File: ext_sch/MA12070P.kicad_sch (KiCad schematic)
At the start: 45 parts, among them J7 Screw Term.

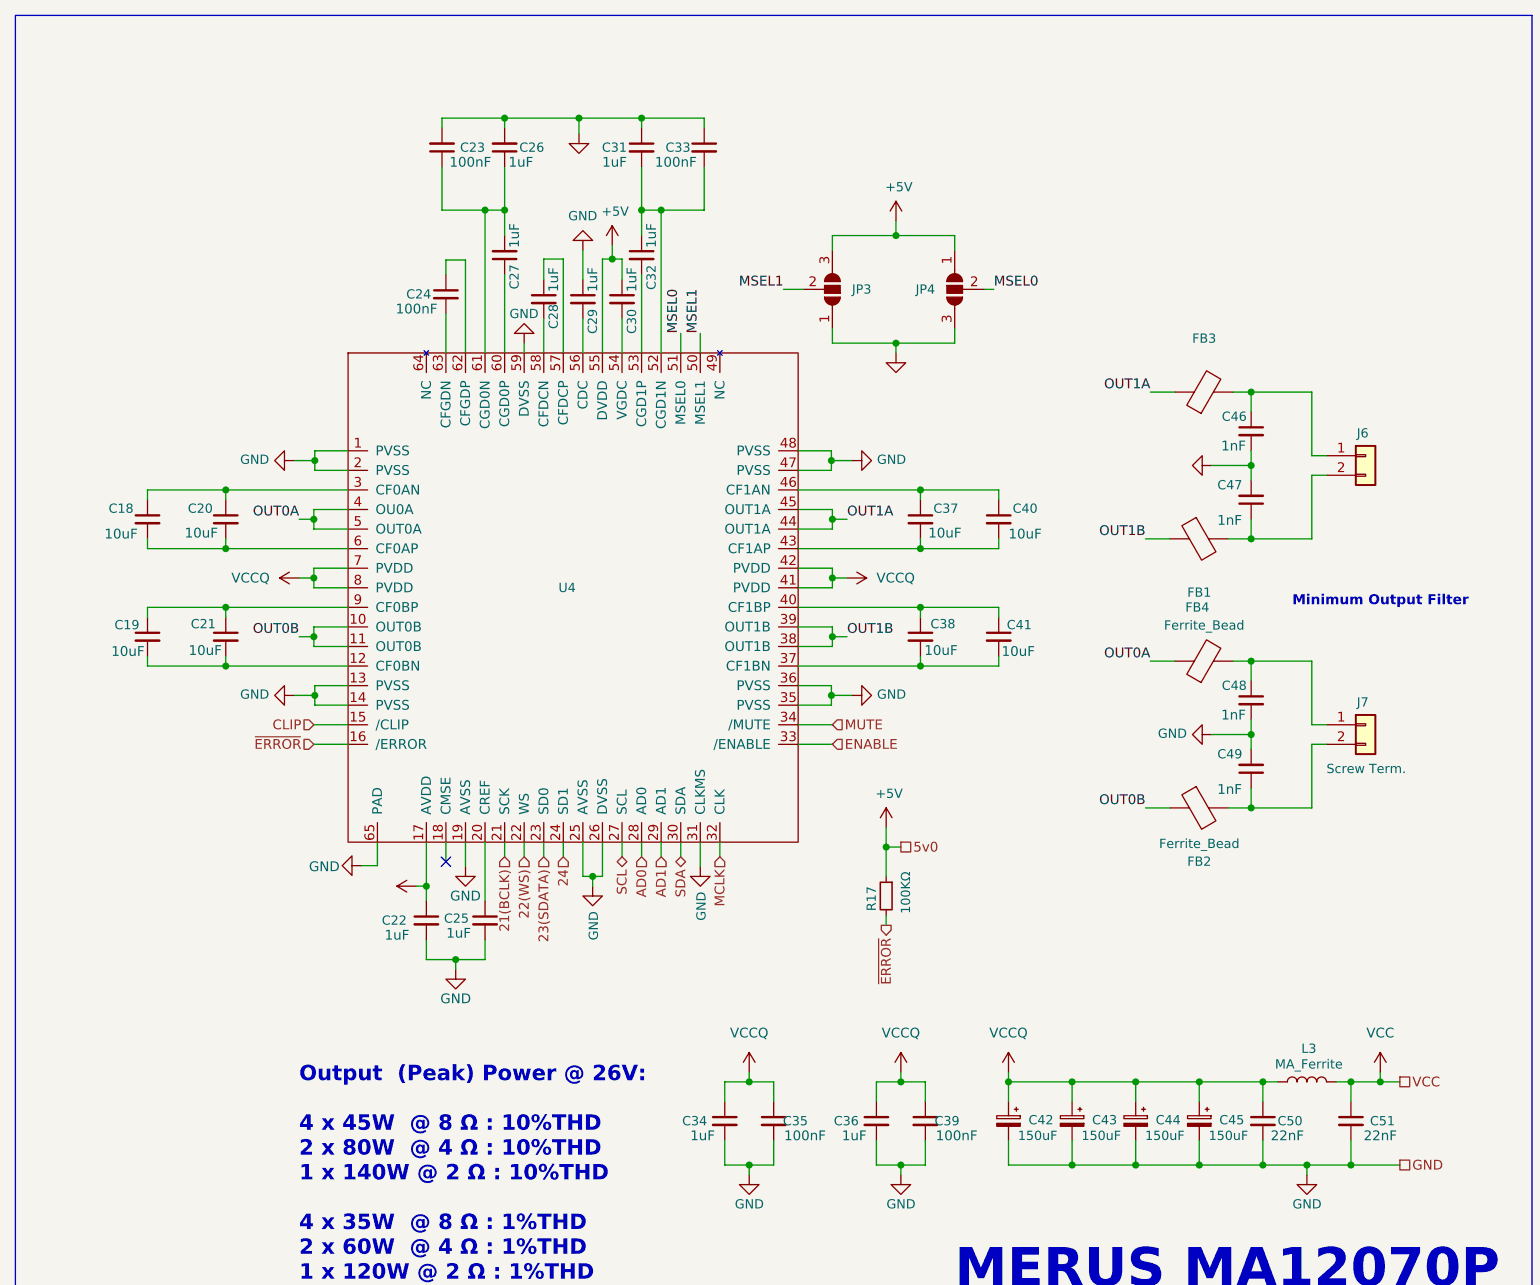
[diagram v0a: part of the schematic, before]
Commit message: Rev04 in the works. New changes include; New DCDC buck, two new connectors, replaced WS-diodes, removed err-diode
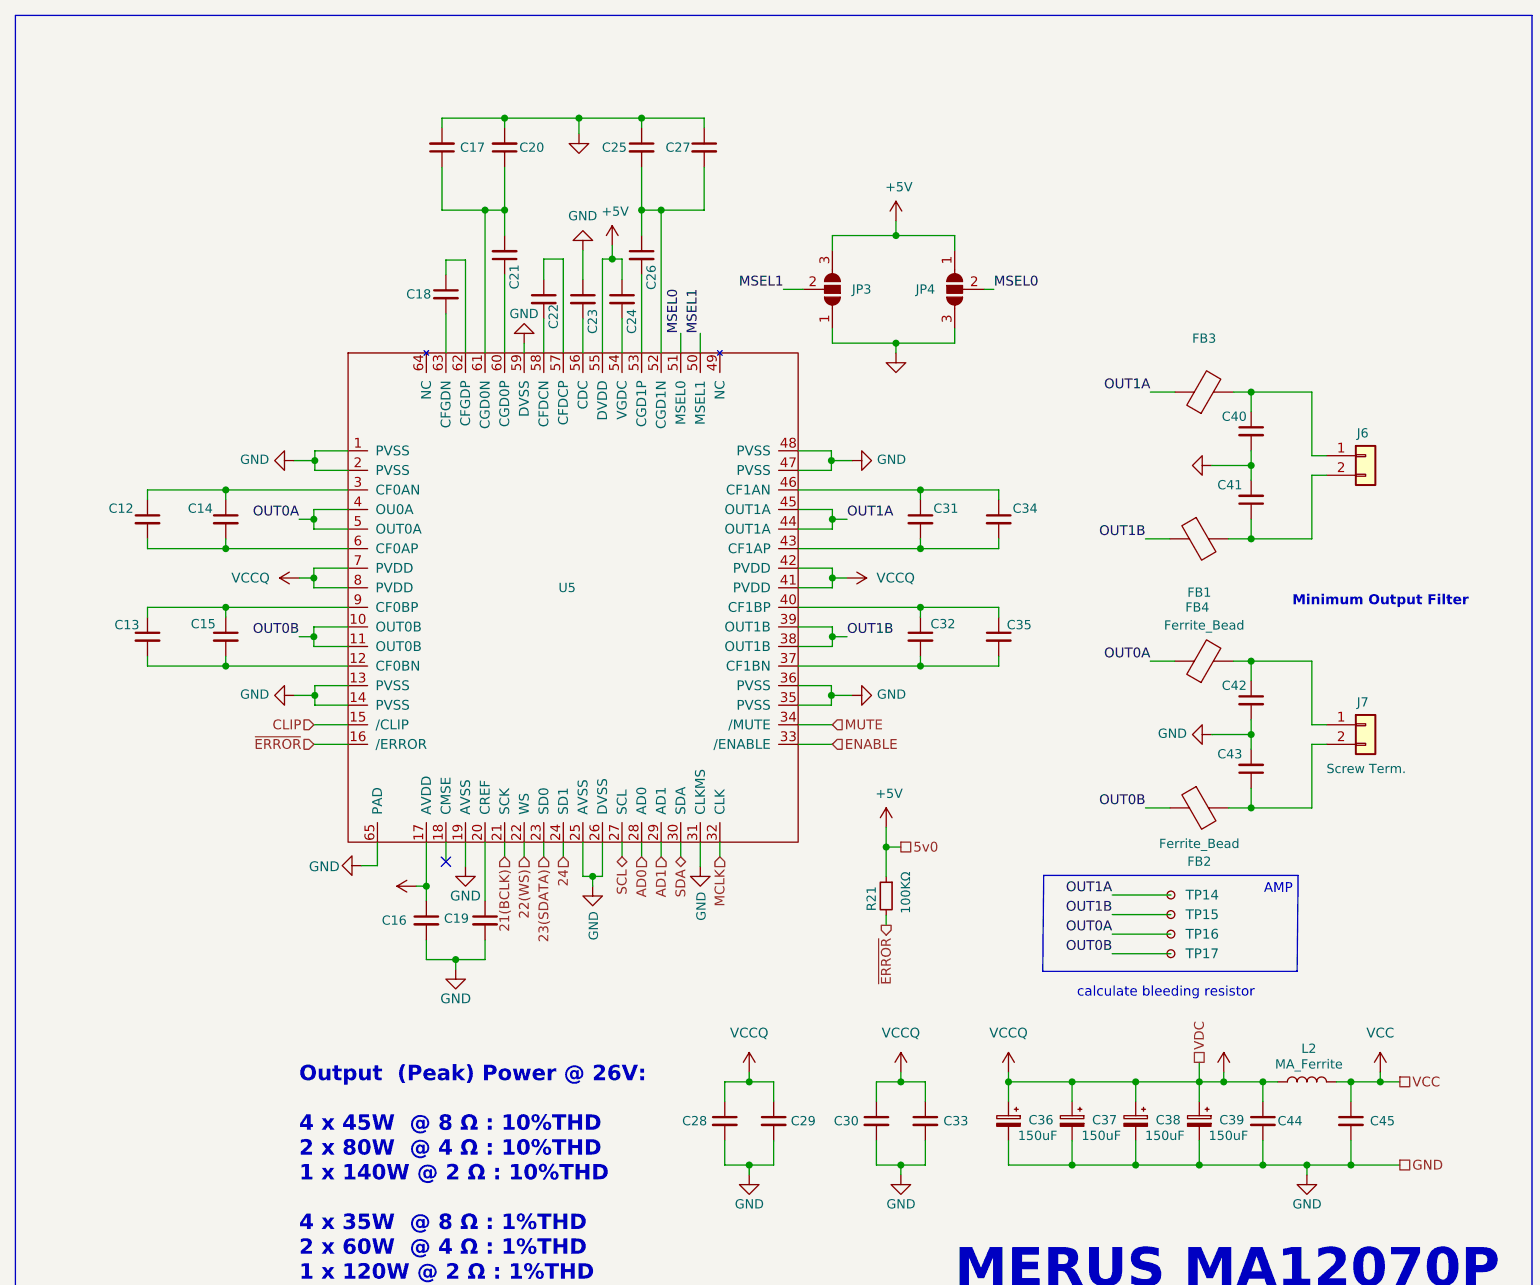
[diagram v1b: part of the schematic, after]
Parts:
- added TP14, TP15, TP16, TP17: TestPoint_Small, TestPoint:TestPoint_Pad_D1.5mm, symbol Connector:TestPoint_Small
- C12: renamed from C18; value CAP_SMD_0805 -> 10uF; VAL 10uF -> (none)
- C13: renamed from C19; value CAP_SMD_0805 -> 10uF; VAL 10uF -> (none)
- C14: renamed from C20; value CAP_SMD_0805 -> 10uF; VAL 10uF -> (none)
- C15: renamed from C21; value CAP_SMD_0805 -> 10uF; VAL 10uF -> (none)
- C16: renamed from C22; value ~ -> 1uF; VAL 1uF -> (none)
- C17: renamed from C23; value ~ -> 100nF; VAL 100nF -> (none)
- C18: renamed from C24; value ~ -> 100nF; VAL 100nF -> (none)
- C19: renamed from C25; value ~ -> 1uF; VAL 1uF -> (none)
- C20: renamed from C26; value ~ -> 1uF; VAL 1uF -> (none)
- C21: renamed from C27; value ~ -> 1uF; VAL 1uF -> (none)
- C22: renamed from C28; value ~ -> 1uF; VAL 1uF -> (none)
- C23: renamed from C29; value ~ -> 1uF; VAL 1uF -> (none)
- C24: renamed from C30; value ~ -> 1uF; VAL 1uF -> (none)
- C25: renamed from C31; value ~ -> 1uF; VAL 1uF -> (none)
- C26: renamed from C32; value ~ -> 1uF; VAL 1uF -> (none)
- C27: renamed from C33; value ~ -> 100nF; VAL 100nF -> (none)
- C28: renamed from C34; value CAP_SMD_0805 -> (none); footprint Capacitor_SMD:C_0805_2012Metric -> (none); VAL 1uF -> (none)
- C29: renamed from C35; value CAP_SMD_0603 -> (none); footprint Capacitor_SMD:C_0603_1608Metric -> (none); VAL 100nF -> (none)
- C30: renamed from C36; value CAP_SMD_0805 -> (none); footprint Capacitor_SMD:C_0805_2012Metric -> (none); VAL 1uF -> (none)
- C31: renamed from C37; value ~ -> 10uF; VAL 10uF -> (none)
- C32: renamed from C38; value ~ -> 10uF; VAL 10uF -> (none)
- C33: renamed from C39; value CAP_SMD_0603 -> (none); footprint Capacitor_SMD:C_0603_1608Metric -> (none); VAL 100nF -> (none)
- C34: renamed from C40; value ~ -> 10uF; VAL 10uF -> (none)
- C35: renamed from C41; value ~ -> 10uF; VAL 10uF -> (none)
- C40: renamed from C46; value ~ -> 1nF; VAL 1nF -> (none)
- C41: renamed from C47; value ~ -> 1nF; VAL 1nF -> (none)
- C42: renamed from C48; value CAP_SMD_0603 -> 1nF; VAL 1nF -> (none)
- C43: renamed from C49; value CAP_SMD_0603 -> 1nF; VAL 1nF -> (none)
- C44: renamed from C50; value CAP_SMD_0603 -> (none); footprint Capacitor_SMD:C_0603_1608Metric -> (none); VAL 22nF -> (none)
- C45: renamed from C51; value ~ -> (none); footprint Capacitor_SMD:C_0603_1608Metric -> (none); VAL 22nF -> (none)
- renumbered C42 to C36, C43 to C37, C44 to C38, C45 to C39, L3 to L2, R17 to R21, U4 to U5
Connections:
- net OUT0A: now also TP16.1
- net OUT0B: now also TP17.1
- net OUT1A: now also TP14.1
- net OUT1B: now also TP15.1
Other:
- note added: "AMP"
- note added: "calculate bleeding resistor"

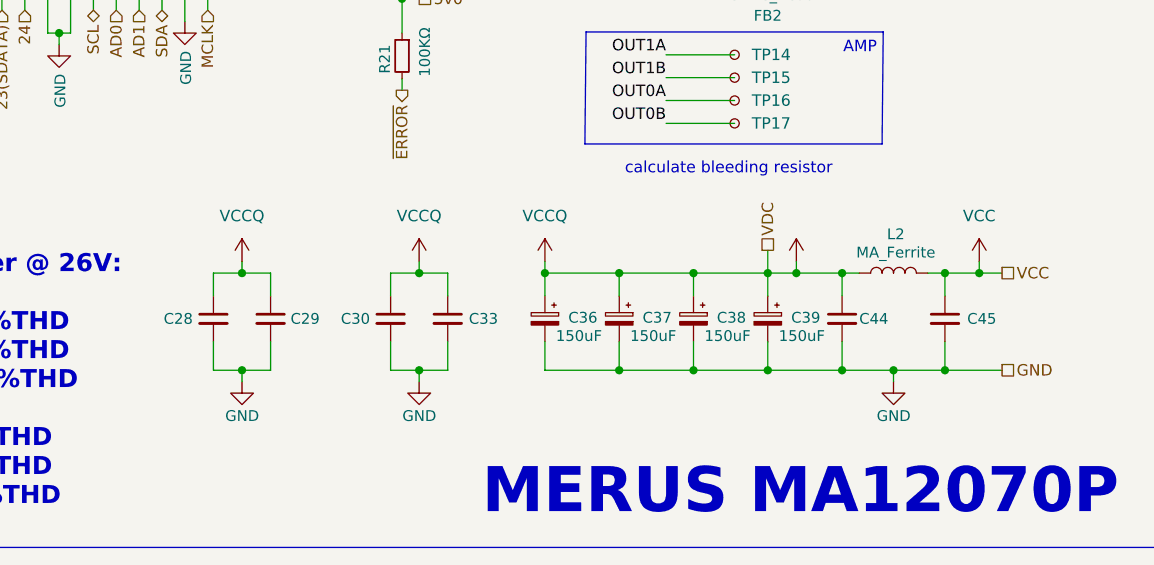
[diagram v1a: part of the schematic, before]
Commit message: fix: Drop voltage on error pin, for mcu read
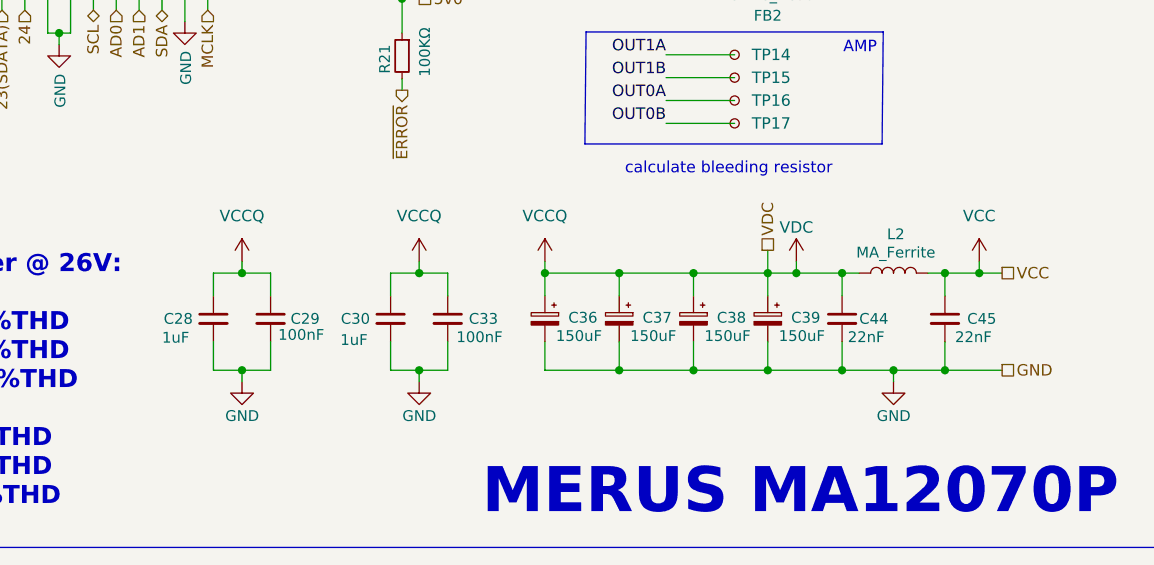
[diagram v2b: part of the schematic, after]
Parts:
- C28, C30: value (none) -> 1uF; footprint (none) -> Capacitor_SMD:C_0805_2012Metric
- C29, C33: value (none) -> 100nF; footprint (none) -> Capacitor_SMD:C_0603_1608Metric
- C44, C45: value (none) -> 22nF; footprint (none) -> Capacitor_SMD:C_0603_1608Metric
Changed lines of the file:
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@@
       (effects (font (size 1.2 1.2)) (justify right))
     )
-    (property "Value" "" (id 1) (at 405.892 267.462 0)
-      (effects (font (size 1.2 1.2)) (justify right))
-    )
-    (property "Footprint" "" (id 2) (at 400.685 265.43 0)
+    (property "Value" "22nF" (id 1) (at 405.892 267.462 0)
+      (effects (font (size 1.2 1.2)) (justify right))
+    )
+    (property "Footprint" "Capacitor_SMD:C_0603_1608Metric" (id 2) (at 400.685 265.43 0)
       (effects (font (size 1.27 1.27)) hide)
     )
@@
       (effects (font (size 1.2 1.2)) (justify right))
     )
-    (property "Value" "" (id 1) (at 331.724 267.208 0)
-      (effects (font (size 1.2 1.2)) (justify right))
-    )
-    (property "Footprint" "" (id 2) (at 325.755 265.43 0)
+    (property "Value" "100nF" (id 1) (at 331.724 267.208 0)
+      (effects (font (size 1.2 1.2)) (justify right))
+    )
+    (property "Footprint" "Capacitor_SMD:C_0603_1608Metric" (id 2) (at 325.755 265.43 0)
       (effects (font (size 1.27 1.27)) hide)
     )
@@
       (effects (font (size 1.2 1.2)) (justify right))
     )
-    (property "Value" "" (id 1) (at 313.69 268.224 0)
+    (property "Value" "1uF" (id 1) (at 313.69 268.224 0)
       (effects (font (size 1.2 1.2)) (justify left bottom))
     )
-    (property "Footprint" "" (id 2) (at 319.405 265.43 0)
+    (property "Footprint" "Capacitor_SMD:C_0805_2012Metric" (id 2) (at 319.405 265.43 0)
       (effects (font (size 1.27 1.27)) hide)
     )
@@
       (effects (font (size 1.2 1.2)) (justify right))
     )
-    (property "Value" "" (id 1) (at 389.89 267.462 0)
-      (effects (font (size 1.2 1.2)) (justify right))
-    )
-    (property "Footprint" "" (id 2) (at 389.255 265.43 0)
+    (property "Value" "22nF" (id 1) (at 389.89 267.462 0)
+      (effects (font (size 1.2 1.2)) (justify right))
+    )
+    (property "Footprint" "Capacitor_SMD:C_0603_1608Metric" (id 2) (at 389.255 265.43 0)
       (effects (font (size 1.27 1.27)) hide)
     )
@@
       (effects (font (size 1.27 1.27)) hide)
     )
-    (property "Value" "" (id 1) (at 384.175 255.27 0))
+    (property "Value" "VDC" (id 1) (at 384.175 255.27 0))
     (property "Footprint" "" (id 2) (at 384.175 259.08 0)
       (effects (font (size 1.27 1.27)) hide)
@@
       (effects (font (size 1.2 1.2)) (justify right))
     )
-    (property "Value" "" (id 1) (at 333.502 268.478 0)
+    (property "Value" "1uF" (id 1) (at 333.502 268.478 0)
       (effects (font (size 1.2 1.2)) (justify left bottom))
     )
-    (property "Footprint" "" (id 2) (at 339.09 265.43 0)
+    (property "Footprint" "Capacitor_SMD:C_0805_2012Metric" (id 2) (at 339.09 265.43 0)
       (effects (font (size 1.27 1.27)) hide)
     )
@@
       (effects (font (size 1.2 1.2)) (justify right))
     )
-    (property "Value" "" (id 1) (at 351.536 267.462 0)
-      (effects (font (size 1.2 1.2)) (justify right))
-    )
-    (property "Footprint" "" (id 2) (at 345.44 265.43 0)
-      (effects (font (size 1.27 1.27)) hide)
-    )
+    (property "Value" "100nF" (id 1) (at 351.536 267.462 0)
+      (effects (font (size 1.2 1.2)) (justify right))
+    )
+    (property "Footprint" "Capacitor_SMD:C_0603_1608Metric" (id 2) (at 345.44 265.43 0)
+      (effects (font (size 1.27 1.27)) hide)
+    )
